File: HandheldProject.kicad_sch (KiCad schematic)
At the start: 16 parts

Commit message: Made lots of good work
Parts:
- added BT1: Battery_Cell, symbol Device:Battery_Cell
- added C1, C2: .47uF, symbol Device:C
- added C3: .1uF, symbol Device:C
- added C4, C5, C6: 1uF, symbol Device:C
- added C7: 470uF, symbol Device:C
- added LS, RS: Speaker, symbol Device:Speaker
- added R10, R11, R12, R13: 10k, symbol Device:R
- added R8, R9: 4 or 8 ohms, symbol Device:R
- added S10, S11, S8, S9: ~, symbol Shakir_Switch_Library:Right_Angle_Switch
- added U2: ~, symbol Shakir_Handheld_Miscellaneous_Library:TP4056_Battery_Charger
- added U3: PCM5102A, Package_SO:TSSOP-20_4.4x6.5mm_P0.65mm, symbol Audio:PCM5102A
- added U4: PAM8403D, Package_SO:SOP-16_3.9x9.9mm_P1.27mm, symbol Amplifier_Audio:PAM8403D
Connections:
- net SCL is gone; now on net SCLK: Raspberry_Pi_Zero_2_W_For_Schematic2.11 (GPIO_11_SCLK_(SPI_0))
- net +3.3V: now also U1.1 (VCC), U1.8 (LED), C5.2, C6.2, C7.2, R10.1, R11.1, R12.1, R13.1, U4.13 (PVDD), U4.4 (PVDD)
- net BCK: now also U3.13 (BCK)
- net CSX: now also U1.3 (CS)
- net DIN: now also U3.14 (DIN)
- net D/CX: now also U1.5 (DC/RS)
- net GND: now also U1.2 (GND), C5.1, C6.1, C7.1, S10.2, S11.2, S8.2, S9.2, U4.15 (PGND), U4.2 (PGND); no longer Raspberry_Pi_Zero_2_W_For_Schematic2.19 (Ground)
- net LCK: now also U3.15 (LRCK)
- net SDI: now also U1.6 (SDI(MOSI))
- net SDO: now also U1.9 (SDO(MISO))
- net SELECT: now also S9.3
- net START: now also S8.3
- net SCLK: now reaches U1.7 (SCK)
- new net: R13.2, S11.1
- new net: C1.2, R8.1
- new net: R12.2, S10.1
- new net: LS.1, U4.1 (LOUT+)
- new net: LS.2, U4.3 (LOUT-)
- new net: C2.2, R9.1
- new net: RS.1, U4.14 (ROUT-)
- new net: RS.2, U4.16 (ROUT+)
- new net: R9.2, U4.10 (INR)
- new net: R11.2, S9.1
- new net: R8.2, U4.7 (INL)
- new net: C3.2, U4.8 (VREF)
- new net: R10.2, S8.1
- new net +3.3VA: C4.2, U4.6 (VDD)
- new net GNDA: C3.1, C4.1, Raspberry_Pi_Zero_2_W_For_Schematic2.19 (Ground), U4.11 (GND)
- new net INL: C1.1, U3.6 (OUTL)
- new net INR: C2.1, U3.7 (OUTR)
- new net MUTESW: S10.3
- new net POWERSW: S11.3
- no-connect marks 19 -> 28
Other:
- note added: "3 Right Angle Buttons"
- note added: "4 Buttons"
- note added: "Analog Ground? The Pin called GND? Or Digital/Power Ground?"
- note added: "Connect LED to 3.3V if you want it to always be bright, and GND if you want it off? Change R (Button) to pin 18 and make 35 PWN pin connect here do this on breadboard!"
- note added: "Don't know if they want 5 or 3.3V but I'll do 3.3 to play it safe"
- note added: "Give a 0 to Mute"
- note added: "Give a 0 to shut it down"
- note added: "I HAVE NO IDEA IF THIS IS RIGHT"
- note added: "INL and INR are Left and Right Channel Input Respectively obv"
- note added: "Not sure this is SCLK or DOUT"
- note added: "Pulse Amplitude Modulation?"
- note added: "Pulse Code Modulation"
- note added: "SDI = Slave Data Input SDO = Slave Data Output For this to make sense"
- note added: "SPI 0 Location"
- note added: "TFT"
- note added: "This Headphone board actually might be pretty confusing"
- note removed: "Fix me just in case"
- moved on the sheet: R1, R2, R3, R4, R5, R6, R7, Raspberry_Pi_Zero_2_W_For_Schematic2, S1, S2, S3, S4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

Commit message: Its so close man!
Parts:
- removed LS, RS: Speaker, symbol Device:Speaker
- added GF1: PAM8403D, symbol Shakir_Handheld_Miscellaneous_Library:PAM8403D
- added LS, RS: Speaker, symbol Shakir_Handheld_Miscellaneous_Library:Speaker_Labeled
- added MCU1: PCM5102A, symbol Shakir_Handheld_Miscellaneous_Library:PCM5102A
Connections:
- net +5V: no longer Raspberry_Pi_Zero_2_W_For_Schematic2.20 (5V)
- net BCK: now also MCU1.7 (BCK)
- net DIN: now also MCU1.8 (DIN)
- net GND: now also U3.10 (DEMP), U3.11 (FLT), U3.12 (SCK), U3.16 (FMT), U3.17 (XSMT); no longer Raspberry_Pi_Zero_2_W_For_Schematic2.34 (Ground)
- net LCK: now also MCU1.9 (LCK)
- new net: GF1.2 (R_out+), RS.1 (Positive)
- new net: GF1.1 (R_out-), RS.2 (Negative)
- new net: GF1.4 (L_out+), LS.1 (Positive)
- new net: GF1.3 (L_out-), LS.2 (Negative)
- new net +5VA: GF1.6 (PWR+(5V)), MCU1.1 (VCC), Raspberry_Pi_Zero_2_W_For_Schematic2.20 (5V)
- new net G (Audio): GF1.8 (G), MCU1.13 (G)
- new net GND1: GF1.5 (PWR-), MCU1.10 (FMT), MCU1.11 (XMT), MCU1.3 (GND), MCU1.4 (FLT), MCU1.5 (DMP), MCU1.6 (SCL), Raspberry_Pi_Zero_2_W_For_Schematic2.34 (Ground)
- new net L (Audio): GF1.7 (L), MCU1.14 (L)
- new net R (Audio): GF1.9 (B), MCU1.12 (R)
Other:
- note added: "5V Analog or Digital?"
- note added: "GND Analog or Digital?"
- moved on the sheet: BT1, U2

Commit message: Its so close man!
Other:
- note added: "Maybe Connect to MUTESW Label"
- note added: "The IC wants 3.3V, but the board wants 5V"
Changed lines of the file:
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@@
+		)
+	)
+	(text "Maybe Connect to\nMUTESW Label"
+		(exclude_from_sim no)
+		(at 129.032 56.642 0)
+		(effects
+			(font
+				(size 1.27 1.27)
+			)
 		)
 	)
@@
 		(exclude_from_sim no)
 		(at 76.708 21.844 0)
+		(effects
+			(font
+				(size 1.27 1.27)
+			)
+		)
+	)
+	(text "The IC wants 3.3V, but the board wants 5V\n"
+		(exclude_from_sim no)
+		(at 119.888 137.414 0)
 		(effects
 			(font
@@
 		(fields_autoplaced yes)
 		(effects
-			(font
-				(size 1.27 1.27)
-			)
-			(justify left bottom)
-		)
-	)
-	(label "3.3V"
-		(at 190.5 107.95 0)
-		(fields_autoplaced yes)
-		(effects

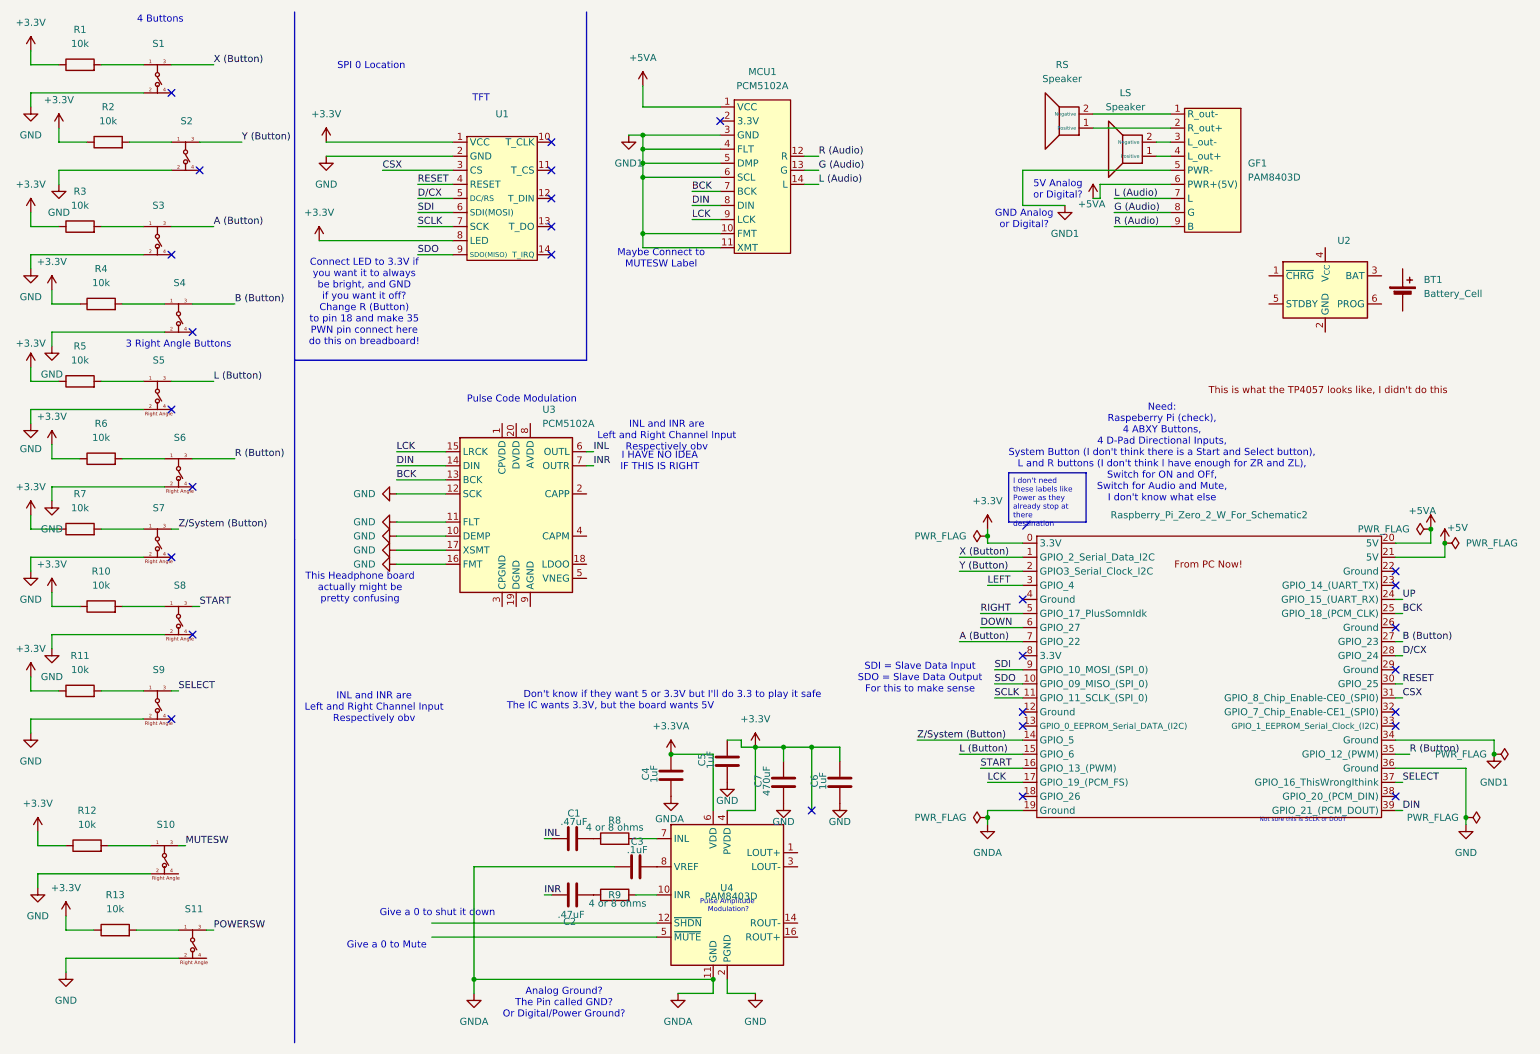
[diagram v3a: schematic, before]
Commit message: I didn't make the pins output that needed to be. I don't have 5V. I just need to learn how to use MUTESW and the other SW
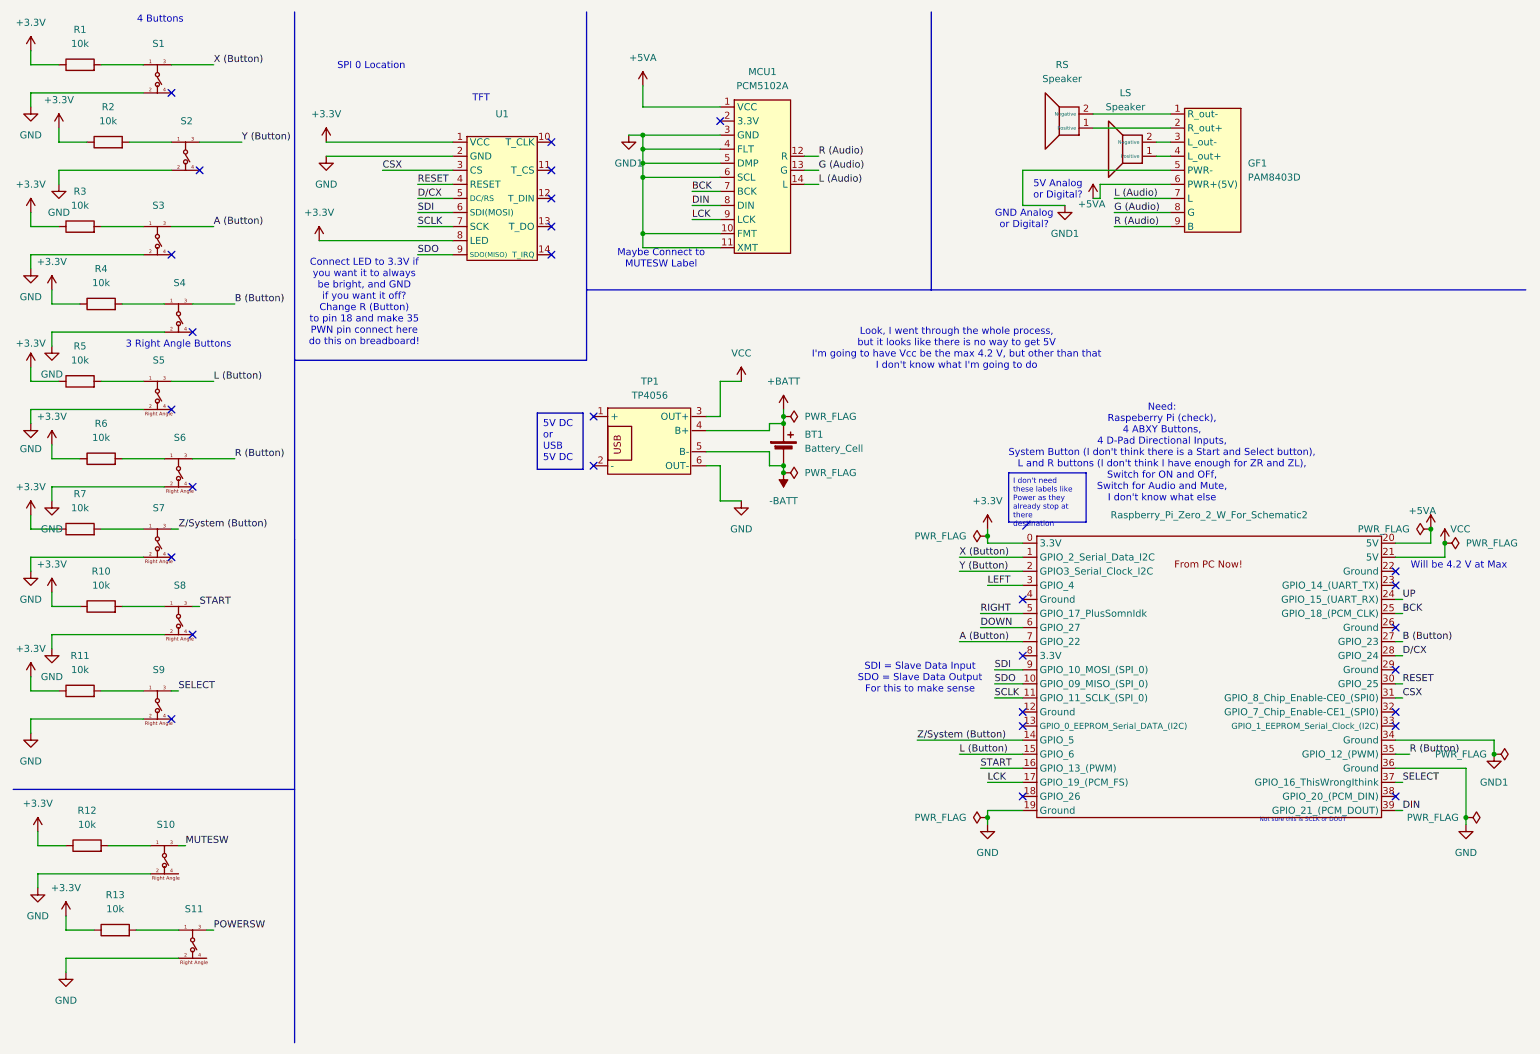
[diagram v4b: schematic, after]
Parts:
- removed C1, C2: .47uF, symbol Device:C
- removed C3: .1uF, symbol Device:C
- removed C4, C5, C6: 1uF, symbol Device:C
- removed C7: 470uF, symbol Device:C
- removed R8, R9: 4 or 8 ohms, symbol Device:R
- removed U2: ~, symbol Shakir_Handheld_Miscellaneous_Library:TP4056_Battery_Charger
- removed U3: PCM5102A, Package_SO:TSSOP-20_4.4x6.5mm_P0.65mm, symbol Audio:PCM5102A
- removed U4: PAM8403D, Package_SO:SOP-16_3.9x9.9mm_P1.27mm, symbol Amplifier_Audio:PAM8403D
- added TP1: TP4056, symbol Shakir_Handheld_Miscellaneous_Library:TP4056
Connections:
- net GNDA is gone; now on net GND: Raspberry_Pi_Zero_2_W_For_Schematic2.19 (Ground)
- net GND: now also TP1.6 (OUT-)
- net +BATT: now reaches BT1.1 (+)
- net +BATT: now also TP1.4 (B+)
- net -BATT: now reaches BT1.2 (-)
- net -BATT: now also TP1.5 (B-)
- net +5V renamed VCC
- net VCC: now also TP1.3 (OUT+)
- no-connect marks 28 -> 29
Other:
- note added: "Look, I went through the whole process, but it looks like there is no way to get 5V I'm going to have Vcc be the max 4.2 V, but other than that I don't know what I'm going to do"
- note added: "Will be 4.2 V at Max"
- note removed: "Analog Ground? The Pin called GND? Or Digital/Power Ground?"
- note removed: "Don't know if they want 5 or 3.3V but I'll do 3.3 to play it safe"
- note removed: "Give a 0 to Mute"
- note removed: "Give a 0 to shut it down"
- note removed: "I HAVE NO IDEA IF THIS IS RIGHT"
- note removed: "INL and INR are Left and Right Channel Input Respectively obv"
- note removed: "Pulse Amplitude Modulation?"
- note removed: "Pulse Code Modulation"
- note removed: "The IC wants 3.3V, but the board wants 5V"
- note removed: "This Headphone board actually might be pretty confusing"

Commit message: Gonna try and prototype today
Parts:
- added S12: ~, symbol Shakir_Switch_Library:Right_Angle_Switch
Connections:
- net GND1: no longer MCU1.11 (XMT)
- net MUTESW: now also MCU1.11 (XMT)
- net VCC: now also S12.3; no longer TP1.3 (OUT+)
- net POWERSW: no longer names the net of S11.3
- new net: S12.2, TP1.3 (OUT+)
- no-connect marks 29 -> 32
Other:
- note added: "TAKE ME AWAY I'm PRETTY SURE"
- note added: "XSMT Pin (Soft Mute / Soft Un-Mute)"
- note added: "YES CONNECT TO MUTESW"
- moved on the sheet: BT1, R13, S11, TP1

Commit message: Added colors for the rats nest I created\
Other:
- note added: "Black"
- note added: "Blue"
- note added: "Brown"
- note added: "Gray"
- note added: "Green"
- note added: "Orange"
- note added: "Purple"
- note added: "Red"
- note added: "Space"
- note added: "White"
- note added: "Yellow"
